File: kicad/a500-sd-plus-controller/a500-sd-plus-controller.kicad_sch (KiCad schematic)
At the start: 3 parts, among them U2 5M160ZE64, U3 SN74LVC8T245, U6 SN74LVC8T245

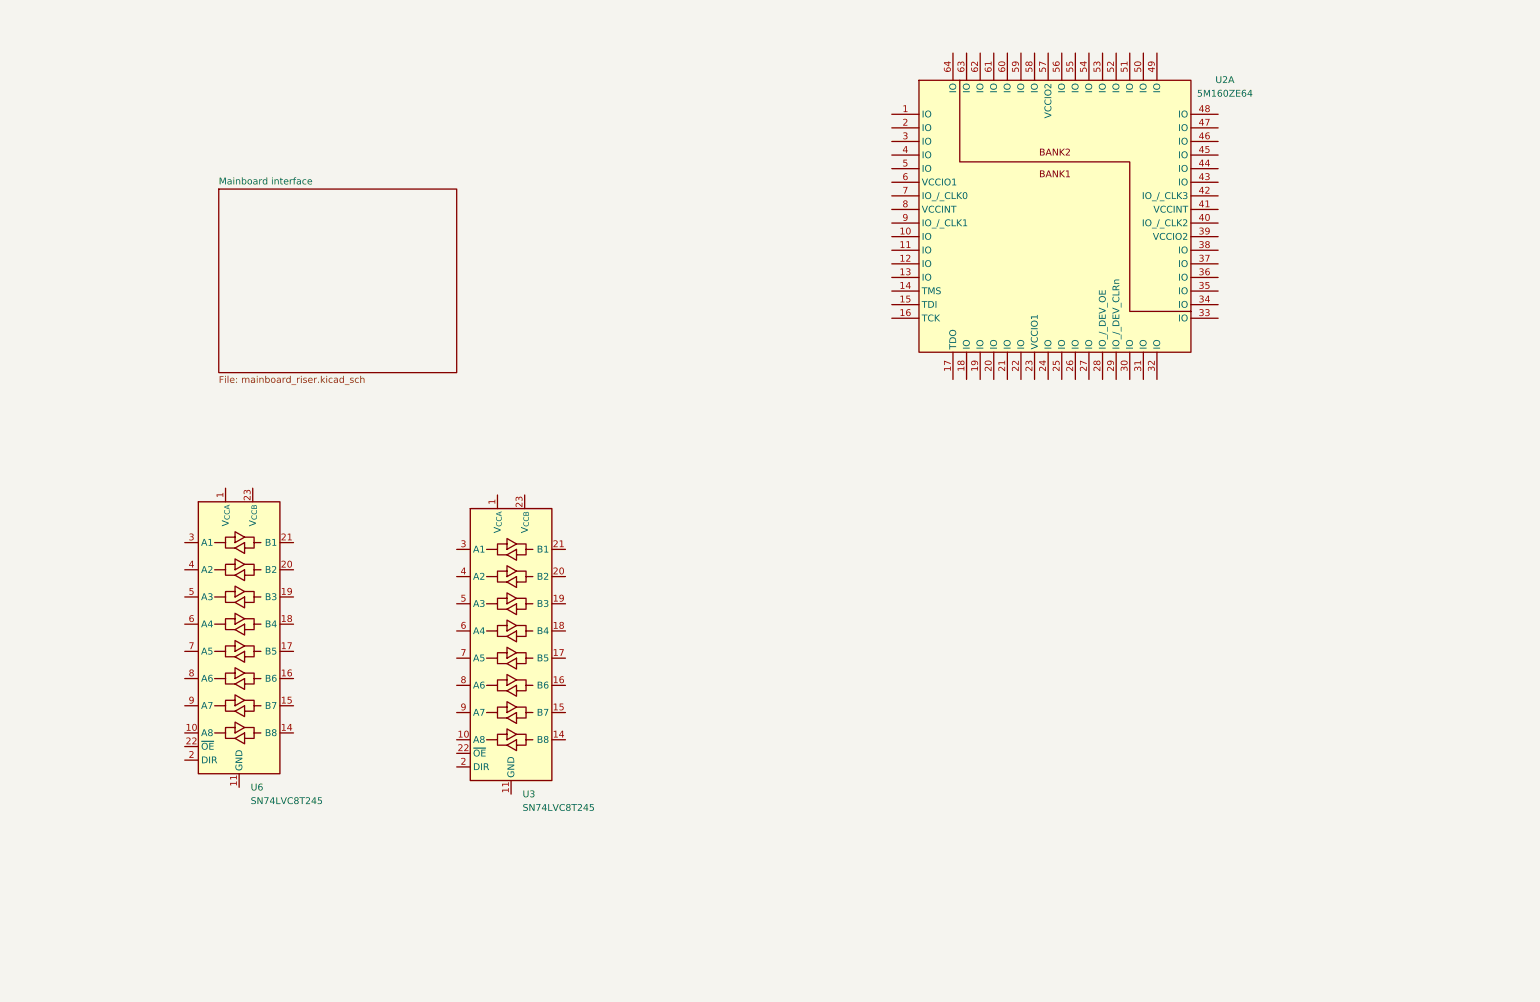
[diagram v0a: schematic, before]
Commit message: more work done on hardware
basic schematic done
layout in progress
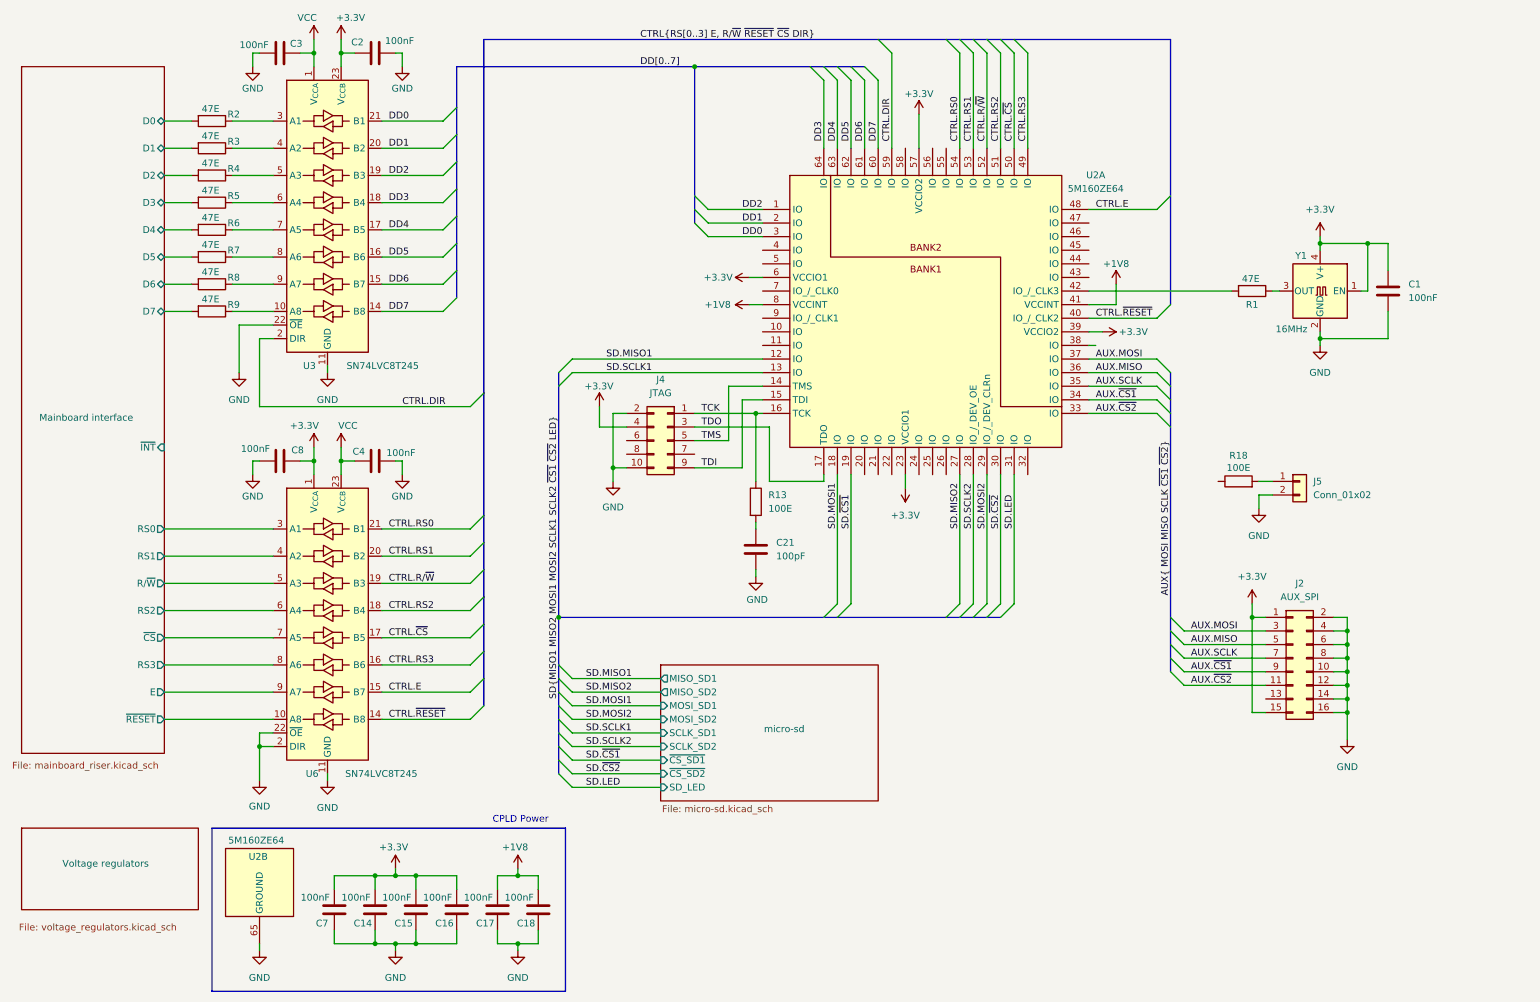
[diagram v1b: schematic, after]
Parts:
- added C1, C14, C15, C16, C17, C18, C2, C3, C4, C7, C8: 100nF, Capacitor_SMD:C_0603_1608Metric, symbol Device:C
- added C21: 100pF, Capacitor_SMD:C_0603_1608Metric, symbol Device:C
- added J2: AUX_SPI, Connector_PinHeader_2.54mm:PinHeader_2x08_P2.54mm_Horizontal, symbol Connector_Generic:Conn_02x08_Odd_Even
- added J4: JTAG, Connector_PinHeader_2.54mm:PinHeader_2x05_P2.54mm_Vertical, symbol Connector_Generic:Conn_02x05_Odd_Even
- added J5: Conn_01x02, Connector_PinHeader_2.54mm:PinHeader_1x02_P2.54mm_Vertical, symbol Connector_Generic:Conn_01x02
- added R1, R2, R3, R4, R5, R6, R7, R8, R9: 47E, Resistor_SMD:R_0603_1608Metric, symbol Device:R
- added R13, R18: 100E, Resistor_SMD:R_0603_1608Metric, symbol Device:R
- added unit 2 of U2
- added Y1: 16MHz, Oscillator:Oscillator_SMD_SeikoEpson_SG210-4Pin_2.5x2.0mm, symbol Oscillator:XO32
- U2: footprint (none) -> Library:EQFP-64_7x7mm_P0.4mm; MPN (none) -> 5M160ZE64I5N
- U3, U6: footprint (none) -> Package_SO:TSSOP-24_4.4x7.8mm_P0.65mm; MPN (none) -> SN74LVC8T245PWR
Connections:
- net DD2: now reaches U2.1 (IO)
- net DD2: now also U3.19 (B3)
- net SD.MISO1: now reaches U2.12 (IO)
- net SD.SCLK1: now reaches U2.13 (IO)
- net TMS: now reaches U2.14 (TMS)
- net TMS: now also J4.5 (Pin_5)
- net TDI: now reaches U2.15 (TDI)
- net TDI: now also J4.9 (Pin_9)
- net TCK: now reaches U2.16 (TCK)
- net TCK: now also J4.1 (Pin_1), R13.1
- net TDO: now reaches U2.17 (TDO)
- net TDO: now also J4.3 (Pin_3)
- net SD.MOSI1: now reaches U2.18 (IO)
- net SD.~{CS1}: now reaches U2.19 (IO)
- net DD1: now reaches U2.2 (IO)
- net DD1: now also U3.20 (B2)
- net +3.3V: now reaches U2.23 (VCCIO1)
- net +3.3V: now also U2.39 (VCCIO2), U2.57 (VCCIO2), U2.6 (VCCIO1), U3.23 (V_{CCB}), U3.24 (V_{CCB}), U6.1 (V_{CCA}), C1.2, C14.1, C15.1, C16.1, C2.2, C7.1, C8.2, J2.1 (Pin_1), J2.15 (Pin_15), J4.4 (Pin_4), Y1.1 (EN), Y1.4 (V+)
- net SD.MISO2: now reaches U2.27 (IO)
- net SD.SCLK2: now reaches U2.28 (IO_/_DEV_OE)
- net SD.MOSI2: now reaches U2.29 (IO_/_DEV_CLRn)
- net DD0: now reaches U2.3 (IO)
- net DD0: now also U3.21 (B1)
- net SD.~{CS2}: now reaches U2.30 (IO)
- net SD.LED: now reaches U2.31 (IO)
- net AUX.~{CS2}: now reaches U2.33 (IO)
- net AUX.~{CS2}: now also J2.11 (Pin_11)
- net AUX.~{CS1}: now reaches U2.34 (IO)
- net AUX.~{CS1}: now also J2.9 (Pin_9)
- net AUX.SCLK: now reaches U2.35 (IO)
- net AUX.SCLK: now also J2.7 (Pin_7)
- net AUX.MISO: now reaches U2.36 (IO)
- net AUX.MISO: now also J2.5 (Pin_5)
- net AUX.MOSI: now reaches U2.37 (IO)
- net AUX.MOSI: now also J2.3 (Pin_3)
- net CTRL.~{RESET}: now reaches U2.40 (IO_/_CLK2)
- net CTRL.~{RESET}: now also U6.14 (B8)
- net +1V8: now reaches U2.41 (VCCINT)
- net +1V8: now also U2.8 (VCCINT), C17.1, C18.1
- net at U2.42 (IO_/_CLK3): now also R1.2
- net CTRL.E: now reaches U2.48 (IO)
- net CTRL.E: now also U6.15 (B7)
- net CTRL.RS3: now reaches U2.49 (IO)
- net CTRL.RS3: now also U6.16 (B6)
- net CTRL.~{CS}: now reaches U2.50 (IO)
- net CTRL.~{CS}: now also U6.17 (B5)
- net CTRL.RS2: now reaches U2.51 (IO)
- net CTRL.RS2: now also U6.18 (B4)
- net CTRL.R/~{W}: now reaches U2.52 (IO)
- net CTRL.R/~{W}: now also U6.19 (B3)
- net CTRL.RS1: now reaches U2.53 (IO)
- net CTRL.RS1: now also U6.20 (B2)
- net CTRL.RS0: now reaches U2.54 (IO)
- net CTRL.RS0: now also U6.21 (B1)
- net CTRL.DIR: now reaches U2.59 (IO)
- net CTRL.DIR: now also U3.2 (DIR)
- net DD7: now reaches U2.60 (IO)
- net DD7: now also U3.14 (B8)
- net DD6: now reaches U2.61 (IO)
- net DD6: now also U3.15 (B7)
- net DD5: now reaches U2.62 (IO)
- net DD5: now also U3.16 (B6)
- net DD4: now reaches U2.63 (IO)
- net DD4: now also U3.17 (B5)
- net DD3: now reaches U2.64 (IO)
- net DD3: now also U3.18 (B4)
- net Mainboard interface/~{RESET}: now reaches U6.10 (A8)
- net GND: now reaches U6.11 (GND), U6.12 (GND), U6.13 (GND)
- net GND: now also U3.11 (GND), U3.12 (GND), U3.13 (GND), U3.22 (~{OE}), U6.2 (DIR), U6.22 (~{OE}), C1.1, C14.2, C15.2, C16.2, C17.2, C18.2, C2.1, C21.1, C3.1, C4.1, C7.2, C8.1, J2.10 (Pin_10), J2.12 (Pin_12), J2.14 (Pin_14), J2.16 (Pin_16), J2.2 (Pin_2), J2.4 (Pin_4), J2.6 (Pin_6), J2.8 (Pin_8), J4.10 (Pin_10), J4.2 (Pin_2), J5.2 (Pin_2), U2.65 (GROUND), Y1.2 (GND)
- net VCC: now reaches U6.23 (V_{CCB}), U6.24 (V_{CCB})
- net VCC: now also U3.1 (V_{CCA}), C3.2, C4.2
- net Mainboard interface/RS0: now reaches U6.3 (A1)
- net Mainboard interface/RS1: now reaches U6.4 (A2)
- net Mainboard interface/R/~{W}: now reaches U6.5 (A3)
- net Mainboard interface/RS2: now reaches U6.6 (A4)
- net Mainboard interface/~{CS}: now reaches U6.7 (A5)
- net Mainboard interface/RS3: now reaches U6.8 (A6)
- net Mainboard interface/E: now reaches U6.9 (A7)
- net at U3.10 (A8): now also R9.1
- net at U3.3 (A1): now also R2.1
- net at U3.4 (A2): now also R3.1
- net at U3.5 (A3): now also R4.1
- net at U3.6 (A4): now also R5.1
- net at U3.7 (A5): now also R6.1
- net at U3.8 (A6): now also R7.1
- net at U3.9 (A7): now also R8.1
- new net: C21.2, R13.2
- new net: J5.1 (Pin_1), R18.2
- new net: R1.1, Y1.3 (OUT)
- new net Mainboard interface/D0: R2.2
- new net Mainboard interface/D1: R3.2
- new net Mainboard interface/D2: R4.2
- new net Mainboard interface/D3: R5.2
- new net Mainboard interface/D4: R6.2
- new net Mainboard interface/D5: R7.2
- new net Mainboard interface/D6: R8.2
- new net Mainboard interface/D7: R9.2
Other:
- added sheet Voltage regulators (voltage_regulators.kicad_sch)
- added sheet micro-sd (micro-sd.kicad_sch)
- sheet Mainboard interface ports: added D0, D1, D2, D3, D4, D5, D6, D7, E, RS0, RS1, RS2, RS3, R/~{W}, ~{CS}, ~{INT}, ~{RESET}; removed none
- note added: "CPLD Power"
- moved on the sheet: U2A, U3, U6

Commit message: added add ethernet controller
still work in progress
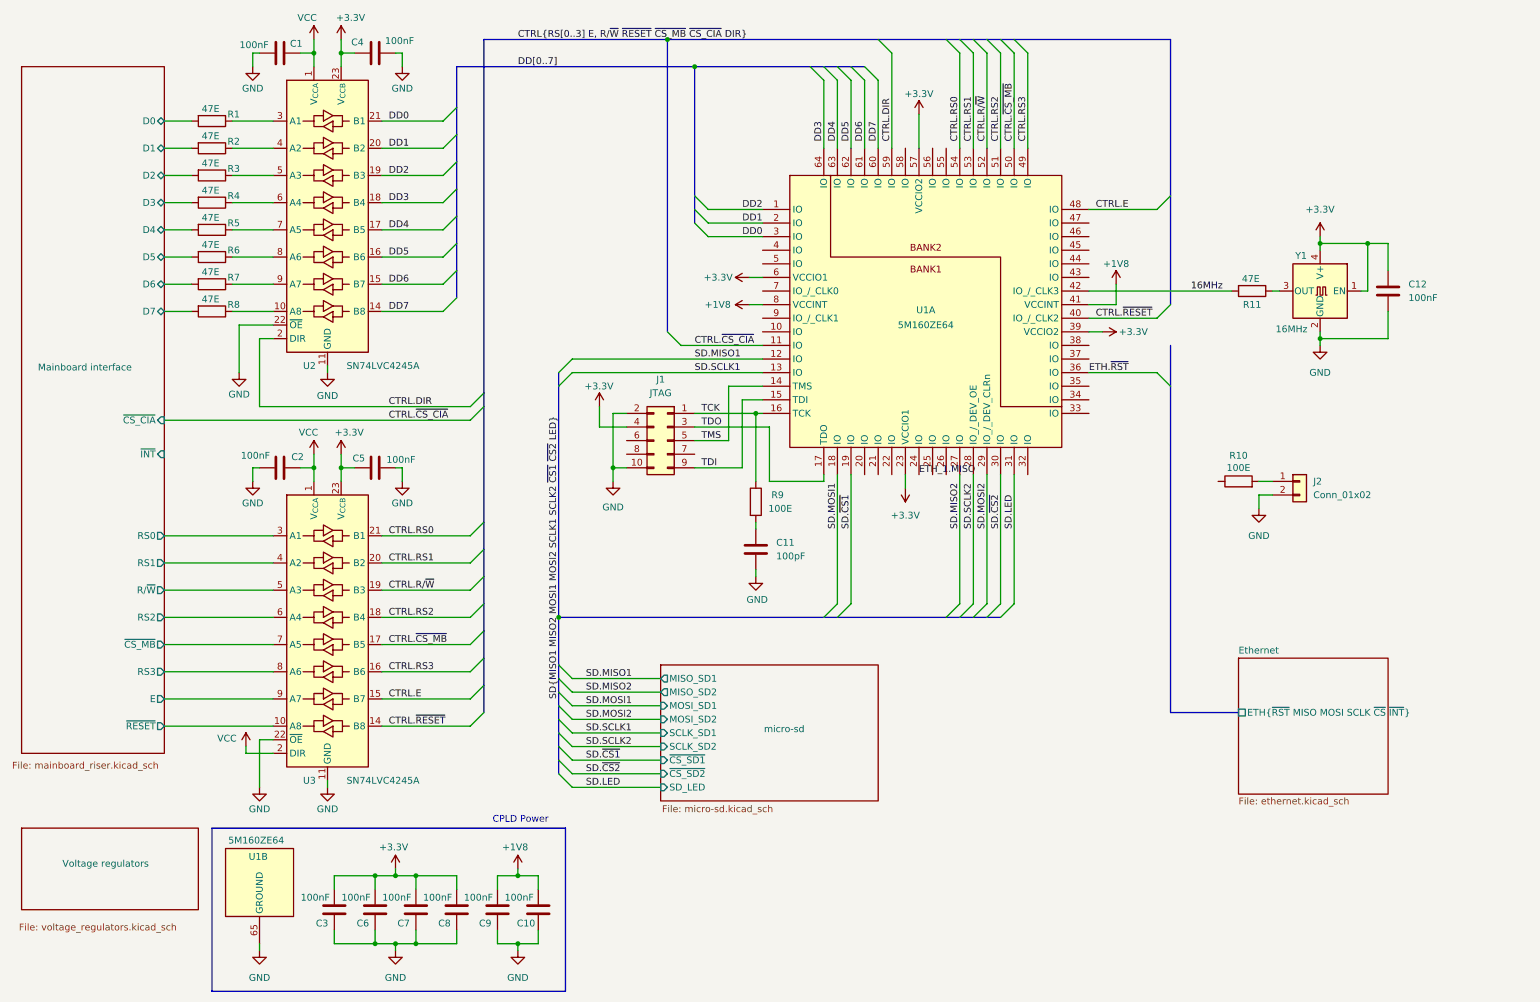
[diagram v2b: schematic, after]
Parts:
- removed J2: AUX_SPI, Connector_PinHeader_2.54mm:PinHeader_2x08_P2.54mm_Horizontal, symbol Connector_Generic:Conn_02x08_Odd_Even
- removed U6: SN74LVC8T245, Package_SO:TSSOP-24_4.4x7.8mm_P0.65mm, symbol Logic_LevelTranslator:SN74LVC8T245
- added U3: SN74LVC4245A, Package_SO:TSSOP-24_4.4x7.8mm_P0.65mm, symbol Logic_LevelTranslator:SN74LVC8T245
- U2: renamed from U3; value SN74LVC8T245 -> SN74LVC4245A; MPN SN74LVC8T245PWR -> SN74LVC4245APWR
- renumbered C3 to C1, C18 to C10, C21 to C11, C1 to C12, C8 to C2, C7 to C3, C2 to C4, C4 to C5, C14 to C6, C15 to C7, C16 to C8, C17 to C9, J4 to J1, J5 to J2, R2 to R1, R18 to R10, R1 to R11, R3 to R2, R4 to R3, R5 to R4, R6 to R5, R7 to R6, R8 to R7, R9 to R8, R13 to R9, U2 to U1
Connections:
- net +3.3V: now also C5.2, U3.23 (V_{CCB}), U3.24 (V_{CCB}); no longer C2.2
- net CTRL.E: now also U3.15 (B7)
- net CTRL.RS0: now also U3.21 (B1)
- net CTRL.RS1: now also U3.20 (B2)
- net CTRL.RS2: now also U3.18 (B4)
- net CTRL.RS3: now also U3.16 (B6)
- net CTRL.R/~{W}: now also U3.19 (B3)
- net CTRL.~{RESET}: now also U3.14 (B8)
- net GND: now also U3.11 (GND), U3.12 (GND), U3.13 (GND), U3.22 (~{OE})
- net Mainboard interface/E: now also U3.9 (A7)
- net Mainboard interface/RS0: now also U3.3 (A1)
- net Mainboard interface/RS1: now also U3.4 (A2)
- net Mainboard interface/RS2: now also U3.6 (A4)
- net Mainboard interface/RS3: now also U3.8 (A6)
- net Mainboard interface/R/~{W}: now also U3.5 (A3)
- net Mainboard interface/~{RESET}: now also U3.10 (A8)
- net VCC: now also C2.2, U3.1 (V_{CCA}), U3.2 (DIR); no longer C5.2
- net CTRL.~{CS_CIA}: now reaches U1.11 (IO)
- net ETH_1.MISO: now reaches U1.24 (IO)
- net 16MHz: now reaches R11.2, U1.42 (IO_/_CLK3)
- net AUX.MISO renamed ETH.~{RST}
- net AUX.MOSI: no longer names the net of U1.37 (IO)
- net AUX.SCLK: no longer names the net of U1.35 (IO)
- net AUX.~{CS1}: no longer names the net of U1.34 (IO)
- net AUX.~{CS2}: no longer names the net of U1.33 (IO)
- net CTRL.~{CS} renamed CTRL.~{CS_MB}
- net CTRL.~{CS_MB}: now also U3.17 (B5)
- new net Mainboard interface/~{CS_MB}: U3.7 (A5)
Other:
- added sheet Ethernet (ethernet.kicad_sch)
- sheet Mainboard interface ports: added ~{CS_CIA}, ~{CS_MB}; removed ~{CS}
- company: Mathesar -> Dennis van Weeren
- title: A500-SD-plus-controller -> A500 SD plus controller
- moved on the sheet: C2, C5

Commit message: routing completely done
todo: review footprints and cleanup silkscreen
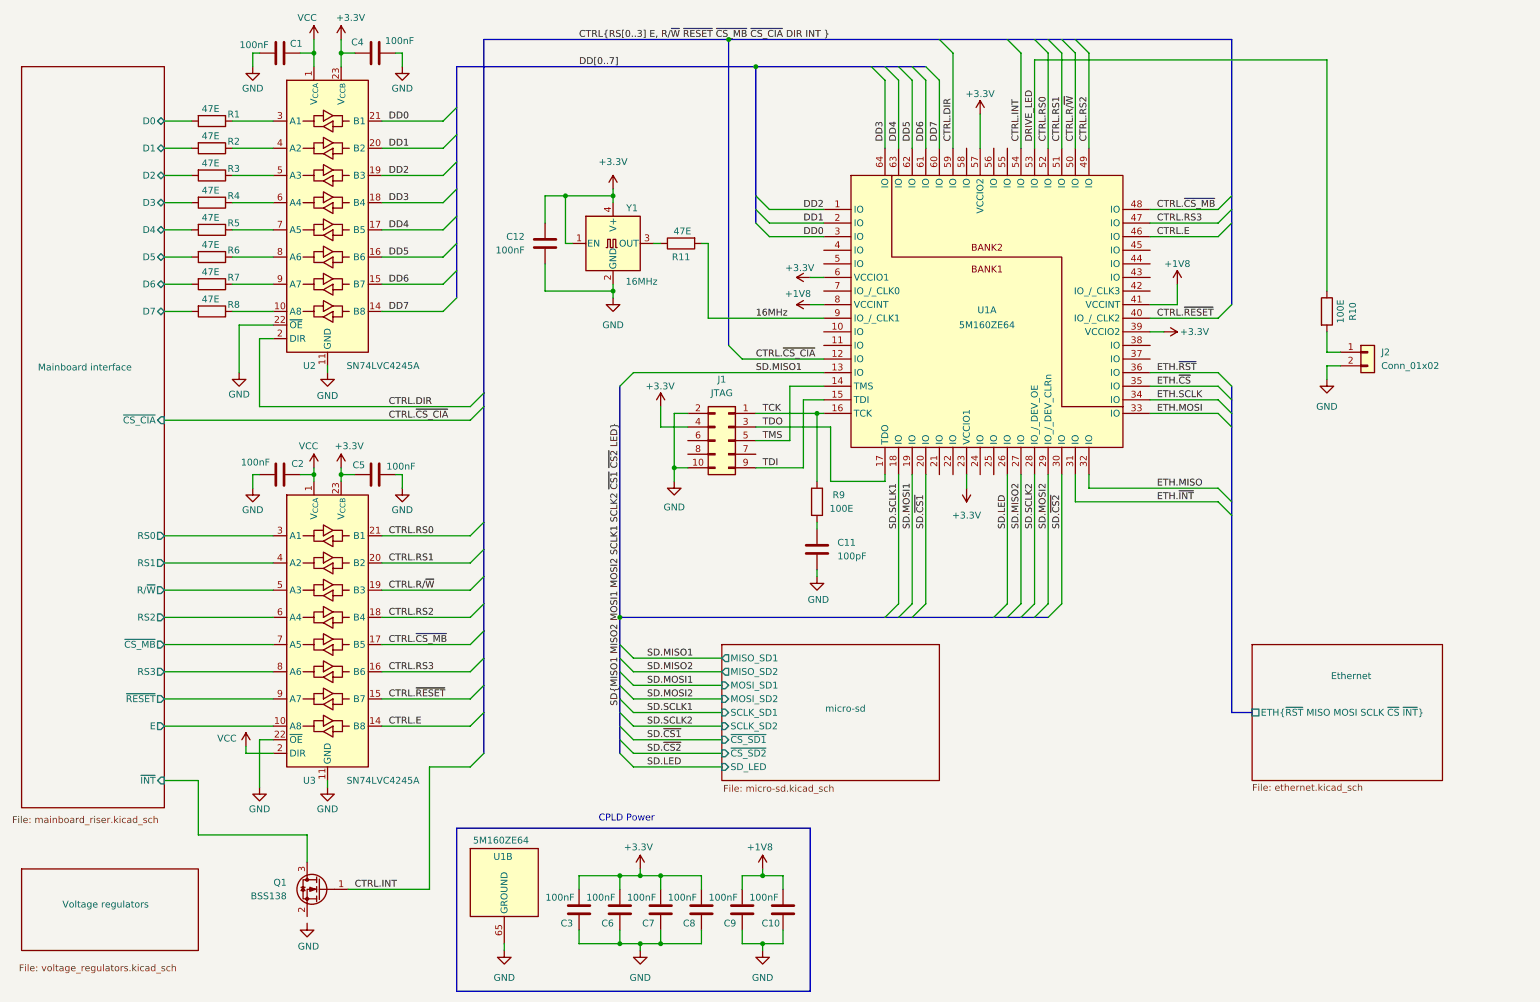
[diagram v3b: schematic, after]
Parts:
- added Q1: BSS138, Package_TO_SOT_SMD:SOT-23, symbol Transistor_FET:BSS138
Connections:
- net 16MHz: now also U1.9 (IO_/_CLK1); no longer U1.42 (IO_/_CLK3)
- net CTRL.E: now also U1.46 (IO), U3.14 (B8); no longer U1.48 (IO), U3.15 (B7)
- net CTRL.RS0: now also U1.52 (IO); no longer U1.54 (IO)
- net CTRL.RS1: now also U1.51 (IO); no longer U1.53 (IO)
- net CTRL.RS2: now also U1.49 (IO); no longer U1.51 (IO)
- net CTRL.RS3: now also U1.47 (IO); no longer U1.49 (IO)
- net CTRL.R/~{W}: now also U1.50 (IO); no longer U1.52 (IO)
- net CTRL.~{CS_CIA}: now also U1.12 (IO); no longer U1.11 (IO)
- net CTRL.~{CS_MB}: now also U1.48 (IO); no longer U1.50 (IO)
- net CTRL.~{RESET}: now also U3.15 (B7); no longer U3.14 (B8)
- net Mainboard interface/E: now also U3.10 (A8); no longer U3.9 (A7)
- net Mainboard interface/~{INT}: now also Q1.3 (D)
- net Mainboard interface/~{RESET}: now also U3.9 (A7); no longer U3.10 (A8)
- net SD.LED: now also U1.26 (IO); no longer U1.31 (IO)
- net SD.MISO1: now also U1.13 (IO); no longer U1.12 (IO)
- net SD.MOSI1: now also U1.19 (IO); no longer U1.18 (IO)
- net SD.SCLK1: now also U1.18 (IO); no longer U1.13 (IO)
- net SD.~{CS1}: now also U1.20 (IO); no longer U1.19 (IO)
- net ETH.MISO: now reaches U1.32 (IO)
- net ETH.MOSI: now reaches U1.33 (IO)
- net ETH.SCLK: now reaches U1.34 (IO)
- net ETH.~{CS}: now reaches U1.35 (IO)
- net DRIVE_LED: now reaches R10.1
- net DRIVE_LED: now also U1.53 (IO)
- net ETH_1.MISO: no longer names the net of U1.24 (IO)
- new net CTRL.INT: Q1.1 (G), U1.54 (IO)
- new net ETH.~{INT}: U1.31 (IO)
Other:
- moved on the sheet: C10, C11, C12, C2, C3, C5, C6, C7, C8, C9, J1, J2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
